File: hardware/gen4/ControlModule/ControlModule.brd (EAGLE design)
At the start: 48.1 x 75.1 mm, 39 parts, among them IC1 XMEGA16A4A

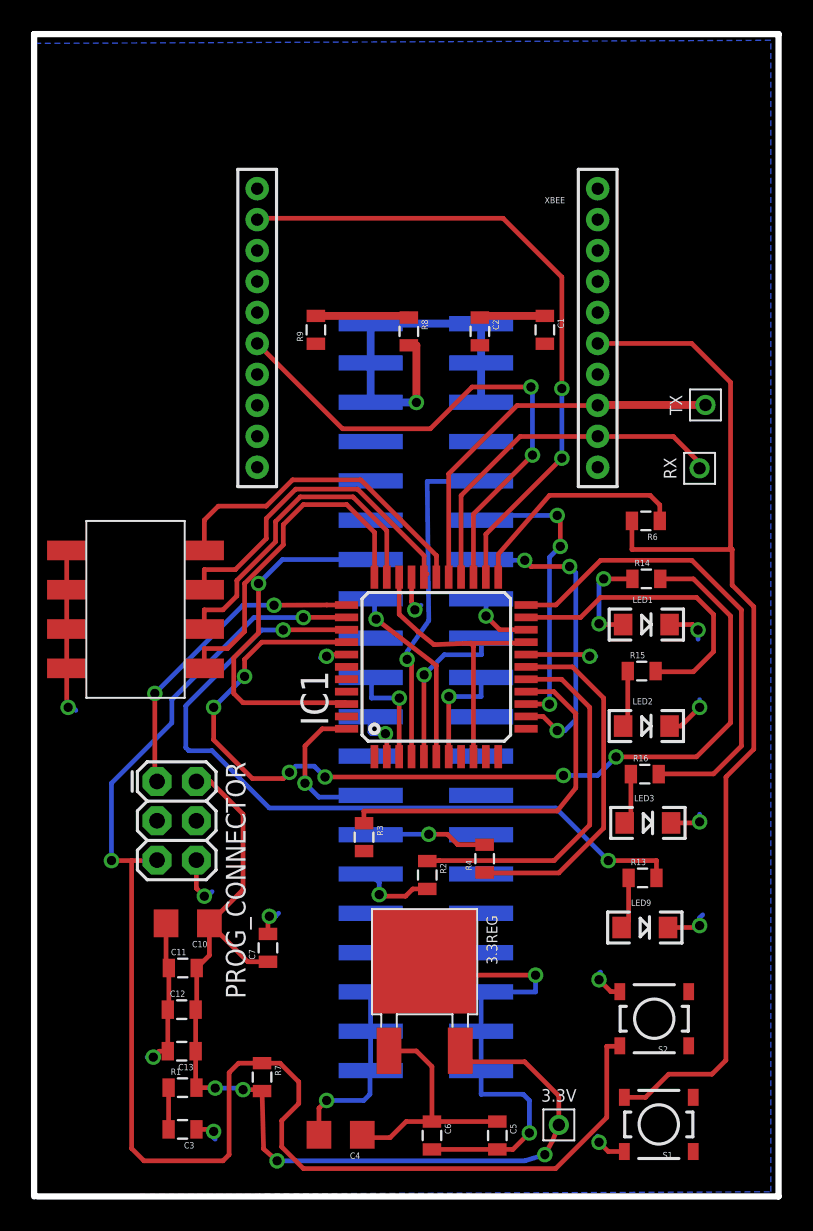
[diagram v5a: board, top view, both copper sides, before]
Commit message: finished routing... still need to do error checking
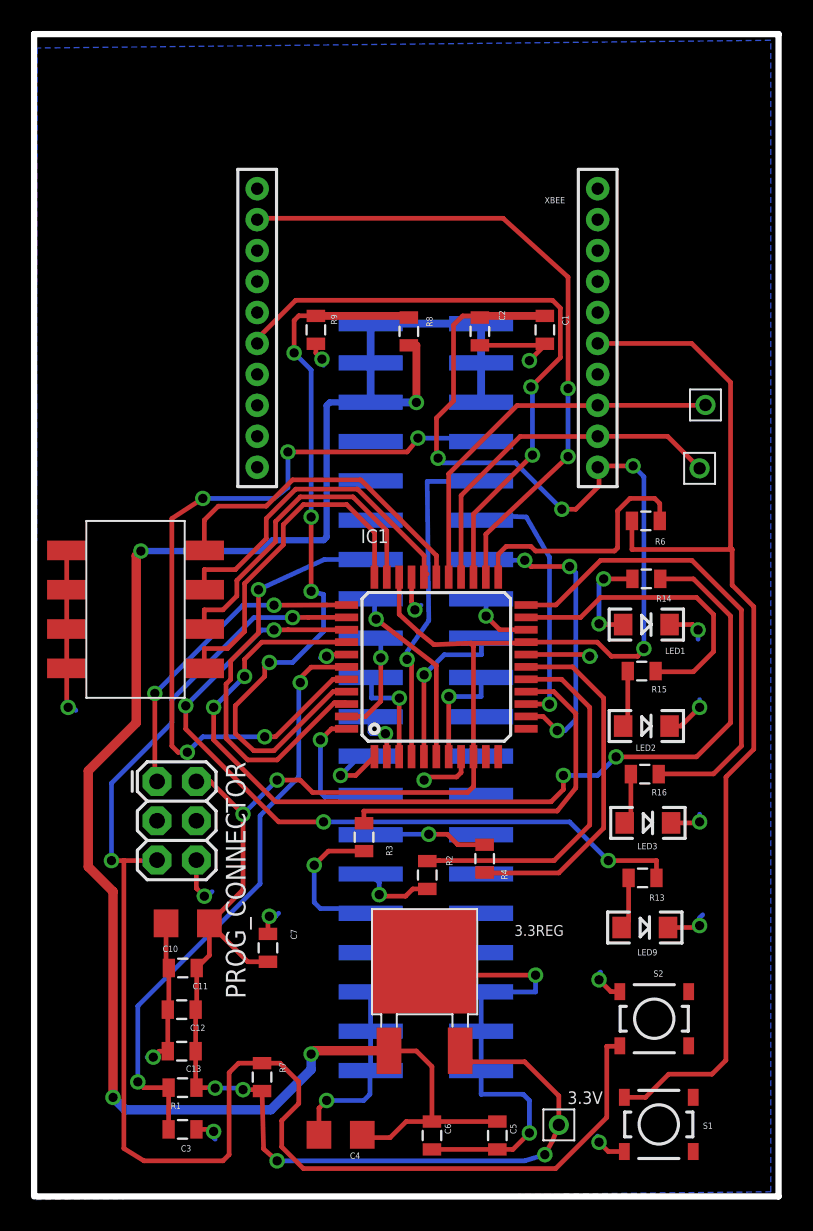
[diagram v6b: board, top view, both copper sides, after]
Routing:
- net 12V: track 40.4 -> 121.9 mm, vias 1 -> 4
- net 3.3V: track 88.9 -> 158.7 mm, vias 4 -> 10
- net BB_IN: track 0.00 -> 51.6 mm, vias 0 -> 5
- net BATSENSE: track 6.11 -> 47.9 mm, vias 0 -> 4
- net N$1: track 2.70 -> 38.6 mm, vias 0 -> 2
- net GND: track 51.7 -> 63.3 mm, vias 14 -> 17
- net N$7: track 0.00 -> 9.94 mm, vias 0 -> 1
- net DRIB: track 0.00 -> 7.45 mm, vias 0 -> 1
- net RTS: track 35.0 -> 40.9 mm
- net SS_3: track 0.00 -> 5.64 mm, vias 0 -> 1
- net DIVCAP: track 23.2 -> 28.1 mm
- net KICK_ENABLE: track 19.1 -> 17.1 mm, vias 3 -> 1
- net SS_4: track 10.2 -> 8.80 mm
- net N$5: track 14.9 -> 16.3 mm
- net RLED1: track 62.0 -> 63.4 mm, vias 6 -> 4
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
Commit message: cleaned up a few things
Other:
- board size 48.1 x 75.1 mm -> 48.2 x 67 mm
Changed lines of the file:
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@@
 <?xml version="1.0" encoding="utf-8"?>
 <!DOCTYPE eagle SYSTEM "eagle.dtd">
-<eagle version="7.4.0">
+<eagle version="7.2.0">
 <drawing>
 <settings>
@@
 <board>
 <plain>
-<wire x1="23.1" y1="74.5" x2="23.1" y2="-0.6" width="0.4064" layer="20"/>
+<wire x1="23.1" y1="66.4" x2="23.1" y2="-0.6" width="0.4064" layer="20"/>
 <wire x1="23.3" y1="-0.6" x2="71.2" y2="-0.6" width="0.4064" layer="20"/>
-<wire x1="71.2" y1="-0.6" x2="71.2" y2="74.5" width="0.4064" layer="20"/>
-<wire x1="71.2" y1="74.5" x2="23.1" y2="74.5" width="0.4064" layer="20"/>
-<dimension x1="73.2" y1="74.5" x2="73.2" y2="-0.6" x3="93.8" y3="36.95" textsize="1.778" layer="20"/>
-<dimension x1="73.2" y1="74.5" x2="23.1" y2="74.5" x3="48.15" y3="86.7" textsize="1.778" layer="20"/>
+<wire x1="71.2" y1="-0.6" x2="71.3" y2="66.4" width="0.4064" layer="20"/>
+<wire x1="71.3" y1="66.4" x2="23.1" y2="66.4" width="0.4064" layer="20"/>
+<dimension x1="72.7" y1="66.6" x2="73.2" y2="-0.6" x3="93.549428125" y3="33.15326875" textsize="1.778" layer="20"/>
+<dimension x1="73.2" y1="74.5" x2="23.1" y2="74.5" x3="48.15" y3="69.2" textsize="1.778" layer="20"/>
 </plain>
 <attributes>
@@
 <vertex x="23.2" y="-0.8"/>
 <vertex x="70.7" y="-0.3"/>
-<vertex x="70.7" y="74.1"/>
-<vertex x="23.3" y="73.6"/>
+<vertex x="70.9" y="66.1"/>
+<vertex x="23.3" y="65.9"/>
 </polygon>
 <wire x1="47.488" y1="39.414" x2="47.488" y2="37.812" width="0.3048" layer="1"/>

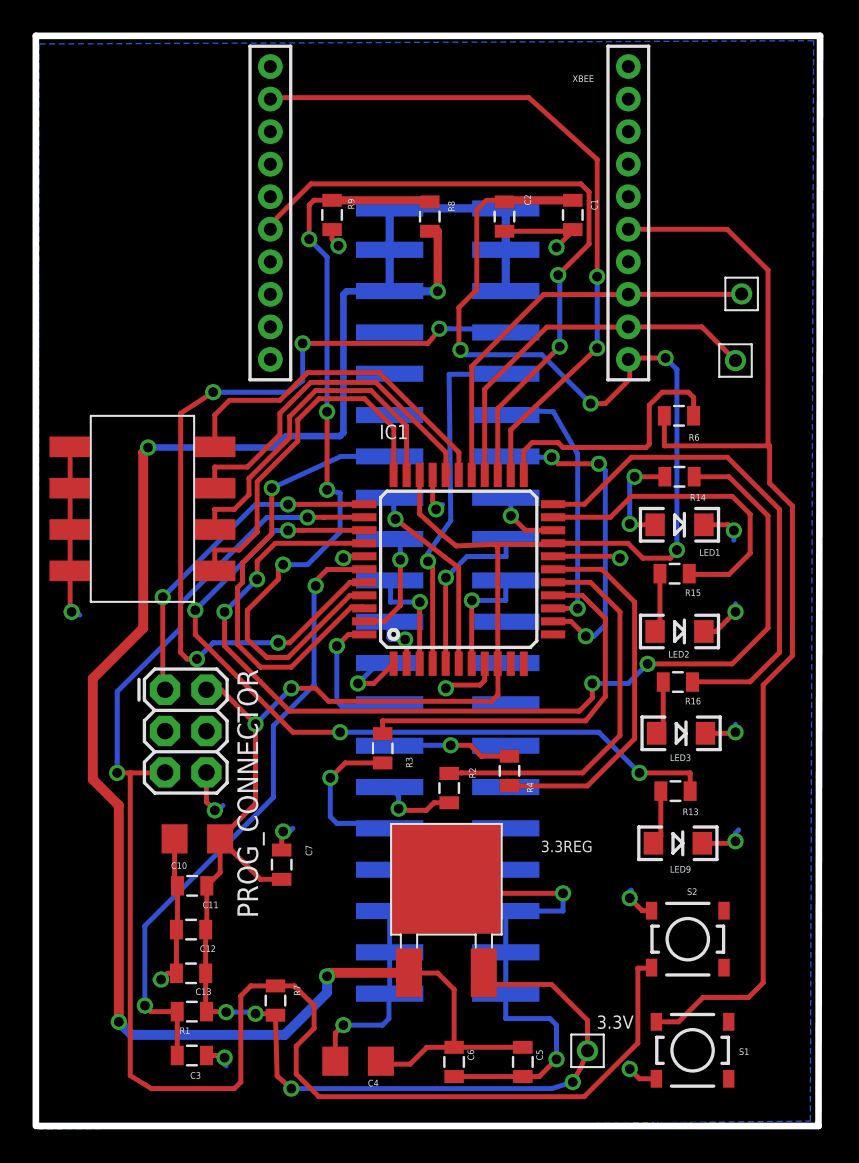
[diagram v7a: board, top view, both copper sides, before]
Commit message: shrunk comms board a bit
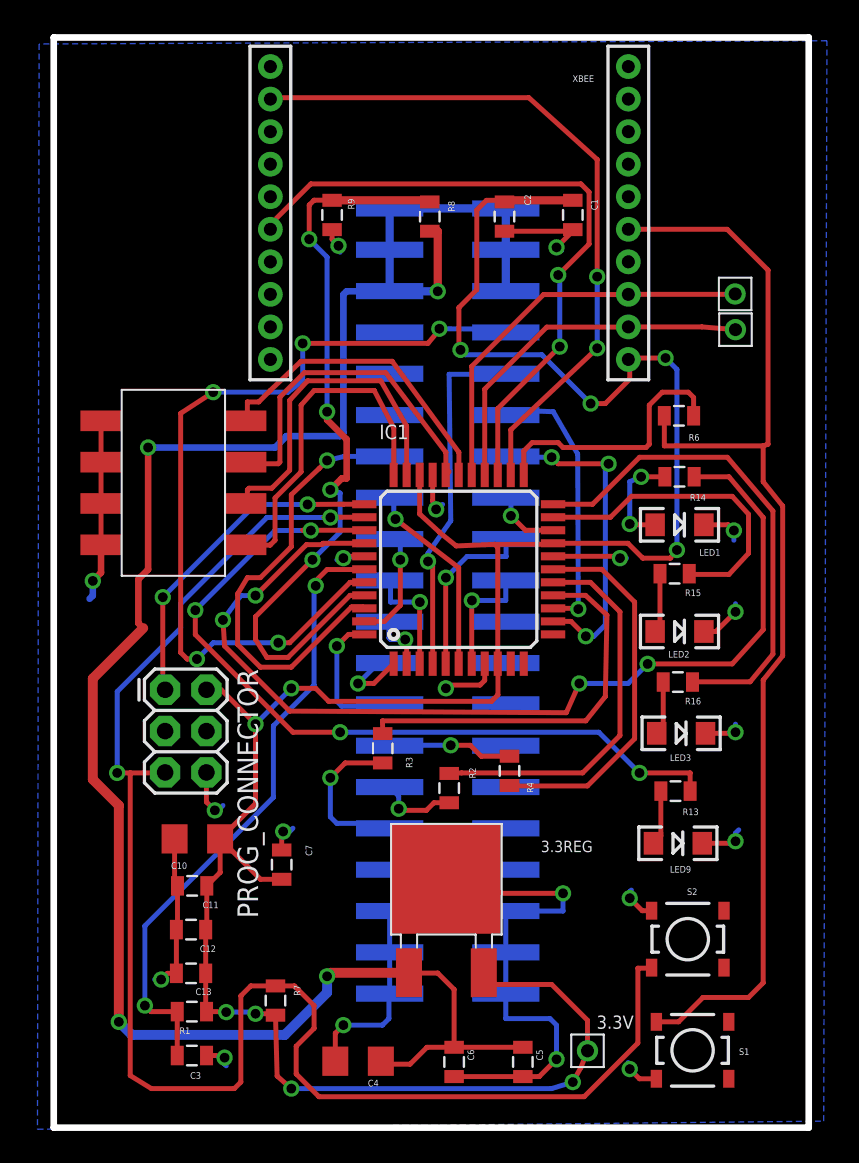
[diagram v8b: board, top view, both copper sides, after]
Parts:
- moved U$1 2.48 mm to (31.6, 38.9)
- moved RX 1.90 mm to (66.1, 48.3)
- moved TX 0.40 mm to (66.1, 50.5)
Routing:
- net BID0: track 21.5 -> 19.4 mm
- net RLED1: track 63.4 -> 62.0 mm
- net RX: track 23.5 -> 22.3 mm
- net BID3: track 22.3 -> 21.3 mm
- net GLED1: track 49.0 -> 49.9 mm
- net RESET: track 97.9 -> 98.6 mm
- net BID1: track 21.9 -> 21.1 mm
- net XBRST: track 70.7 -> 70.0 mm
- net BID2: track 21.3 -> 20.6 mm
- net RLED2: track 31.3 -> 30.8 mm
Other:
- board size 48.2 x 67 mm -> 46.4 x 67 mm
